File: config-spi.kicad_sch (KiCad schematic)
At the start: 40 parts, among them J1 878321412, Q7 BSS138APW, Q8 BSS138APW, U15 XC7K160T-FFG676, U3 S25FL128SAGNFI000

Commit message: Rebase to Rev. 1.2.2
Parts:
- removed C12: C_47u_0603, data-center-dram-tester-footprints:0603-cap, symbol data-center-dram-tester:C_47u_0603
- removed C13, C37: C_470n_0402, data-center-dram-tester-footprints:0402-cap, symbol data-center-dram-tester:C_470n_0402
- removed C5: C_100n_0402, antmicro-footprints:0402-cap, symbol antmicroCapacitors0402:C_100n_0402
- removed D1, D10: KP-1608CGCK, data-center-dram-tester-footprints:LED_0603, symbol data-center-dram-tester:KP-1608CGCK
- removed D4: TPD6E05U06, data-center-dram-tester-footprints:TPD6E05U06, symbol data-center-dram-tester:TPD6E05U06
- removed EMCCLK1, PUDC_B1: TP_SMD1MM, data-center-dram-tester-footprints:Testpoint_smd_1mm, symbol data-center-dram-tester:TP_SMD1MM
- removed J1: 878321412, antmicro-footprints:PinHeader_2x7_P2mm_SMD_no_locator, symbol antmicroRectangularConnectorsHeadersMalePins:878321412
- removed PROG_B1: B3U-1000P, data-center-dram-tester-footprints:Switch_Tactile_SMD_B3U-1000P, symbol data-center-dram-tester:B3U-1000P
- removed Q7, Q8: BSS138APW, data-center-dram-tester-footprints:SC70-3, symbol data-center-dram-tester:BSS138APW
- removed R10, R33, R34, R36: R_100R_0402, data-center-dram-tester-footprints:0402-res, symbol data-center-dram-tester:R_100R_0402
- removed R11, R12, R13, R23, R24, R26, R27, R58, R59, R60, R9: R_0R_0402, data-center-dram-tester-footprints:0402-res, symbol data-center-dram-tester:R_0R_0402
- removed R14: R_2k2_0402, data-center-dram-tester-footprints:0402-res, symbol data-center-dram-tester:R_2k2_0402
- removed R193: R_10k_0402, antmicro-footprints:0402-res, symbol antmicroResistors0402:R_10k_0402
- removed R21, R22, R28, R32: R_4k7_0402, data-center-dram-tester-footprints:0402-res, symbol data-center-dram-tester:R_4k7_0402
- removed R30, R31, R57: R_330R_0402, data-center-dram-tester-footprints:0402-res, symbol data-center-dram-tester:R_330R_0402
- removed S2: DS04-254-1-01BK-SMT, antmicro-footprints:SW_DS04-254-1-01BK-SMT, symbol antmicroSlideSwitches:DS04-254-1-01BK-SMT
- removed U15: XC7K160T-FFG676, antmicro-footprints:xc7k160tfbg676, symbol data-center-dram-tester:XC7K160T-FFG676
- removed U3: S25FL128SAGNFI000, antmicro-footprints:WSON8x6_WSON6x5_dual, symbol data-center-dram-tester:S25FL128SAGNFI000
- added C12: C_47u_0603, data-center-rdimm-ddr4-tester-footprints:C_0603_1608Metric, symbol data-center-rdimm-ddr4-tester:C_47u_0603
- added C13, C37: C_470n_0402, data-center-rdimm-ddr4-tester-footprints:C_0402_1005Metric, symbol data-center-rdimm-ddr4-tester:C_470n_0402
- added C5: C_100n_0402, data-center-rdimm-ddr4-tester-footprints:C_0402_1005Metric, symbol data-center-rdimm-ddr4-tester:C_100n_0402
- added D1, D10: LED_G_0603_KP-1608CGCK, data-center-rdimm-ddr4-tester-footprints:LED_0603_1608Metric_G, symbol data-center-rdimm-ddr4-tester:LED_G_0603_KP-1608CGCK
- added D4: TPD6E05U06RVZR, data-center-rdimm-ddr4-tester-footprints:USON-14_3.5X1.3X0.5mm_P0.5mm, symbol data-center-rdimm-ddr4-tester:TPD6E05U06RVZR
- added EMCCLK1, PUDC_B1: TP_1mm_SMD, data-center-rdimm-ddr4-tester-footprints:Testpoint_smd_1mm, symbol data-center-rdimm-ddr4-tester:TP_1mm_SMD
- added J1: PinHeader_2x7_P2mm_SMD_Shrouded_no-locator, data-center-rdimm-ddr4-tester-footprints:PinHeader_2x7_P2mm_SMD_Shrouded_no-locator, symbol data-center-rdimm-ddr4-tester:PinHeader_2x7_P2mm_SMD_Shrouded_no-locator
- added PROG_B1: SW_B3U-1000P, data-center-rdimm-ddr4-tester-footprints:SW_B3U-3000P, symbol data-center-rdimm-ddr4-tester:SW_B3U-1000P
- added Q7, Q8: BSS138PW, data-center-rdimm-ddr4-tester-footprints:SC70-3, symbol data-center-rdimm-ddr4-tester:BSS138PW
- added R10, R33, R34, R36: R_100R_0402, data-center-rdimm-ddr4-tester-footprints:R_0402_1005Metric, symbol data-center-rdimm-ddr4-tester:R_100R_0402
- added R11, R12, R13, R23, R24, R26, R27, R58, R59, R60, R9: R_0R_0402, data-center-rdimm-ddr4-tester-footprints:R_0402_1005Metric, symbol data-center-rdimm-ddr4-tester:R_0R_0402
- added R14: R_2k2_0402, data-center-rdimm-ddr4-tester-footprints:R_0402_1005Metric, symbol data-center-rdimm-ddr4-tester:R_2k2_0402
- added R193: R_10k_0402, data-center-rdimm-ddr4-tester-footprints:R_0402_1005Metric, symbol data-center-rdimm-ddr4-tester:R_10k_0402
- added R21, R22, R28, R32: R_4k7_0402, data-center-rdimm-ddr4-tester-footprints:R_0402_1005Metric, symbol data-center-rdimm-ddr4-tester:R_4k7_0402
- added R30, R31, R57: R_330R_0402, data-center-rdimm-ddr4-tester-footprints:R_0402_1005Metric, symbol data-center-rdimm-ddr4-tester:R_330R_0402
- added S2: SW_DS04-254-1-01BK-SMT, data-center-rdimm-ddr4-tester-footprints:SW_DS04-254-1-01BK-SMT, symbol data-center-rdimm-ddr4-tester:SW_DS04-254-1-01BK-SMT
- added U15: XC7K160T-FFG676, data-center-rdimm-ddr4-tester-footprints:BGA-676_27x27mm_Layout26x26_P1X1mm, symbol data-center-rdimm-ddr4-tester:XC7K160T-FFG676
- added U3: S25FL128SAGNFI000, data-center-rdimm-ddr4-tester-footprints:WSON-8_6x8x0.5mm_P1.27mm, symbol data-center-rdimm-ddr4-tester:S25FL128SAGNFI000
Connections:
- net 3V3_SYS: now also C12.1, C13.1, C37.1, C5.1, D1.1, D10.1, J1.2, R10.1, R12.2, R14.1, R193.2, R21.1, R22.1, R28.1, R32.1, R33.1, R57.1, R58.1, R9.2, U15.L7 (VCCO_0), U15.T6 (VCCO_0), U3.8 (V_{CC})
- net CCLK: now also R24.2, R33.2, R34.1, U15.C8 (CCLK_0)
- net CFGBVS: now also R58.2, U15.P7 (CFGBVS_0)
- net DONE: now also Q7.1 (G), R57.2, U15.J7 (DONE_0)
- net EMCCLK: now also EMCCLK1.1
- net FCS_B: now also R14.2, R23.2
- net GND: now also C12.2, C13.2, C37.2, C5.2, D4.10 (GND), D4.5 (GND), J1.1, J1.11, J1.13, J1.3, J1.5, J1.7, J1.9, PROG_B1.2, Q7.2 (S), Q8.2 (S), R11.2, R13.2, R34.2, R36.2, S2.2, U15.N11 (VREFN_0), U15.N12 (VP_0), U15.P11 (VN_0), U15.P12 (VREFP_0), U15.R11 (DXN_0), U15.R12 (DXP_0), U3.4 (V_{SS})
- net INIT_B: now also Q8.1 (G), R28.2, U15.G7 (INIT_B_0)
- net MODE0: now also R11.1, R9.1, U15.T5 (M0_0)
- net MODE1: now also R12.1, R13.1, U15.T2 (M1_0)
- net MODE2: now also R193.1, S2.1, U15.P5 (M2_0)
- net PROGRAM_B: now also PROG_B1.1, R32.2, U15.P6 (PROGRAM_B_0)
- net PUDC_B: now also PUDC_B1.1, R10.2, R36.1
- net QSPI_DQ0: now also R59.2
- net QSPI_DQ1: now also R60.2
- net QSPI_DQ2: now also R22.2, R27.2
- net QSPI_DQ3: now also R21.2, R26.2
- net TCK_JTAG: now also D4.13 (D1-), D4.2 (D1-), J1.6, U15.L8 (TCK_0)
- net TDI_JTAG: now also D4.7 (D3-), D4.8 (D3-), J1.10, U15.R6 (TDI_0)
- net TDO_JTAG: now also D4.6 (D3+), D4.9 (D3+), J1.8, U15.R7 (TDO_0)
- net TMS_JTAG: now also D4.1 (D1+), D4.14 (D1+), J1.4, U15.N8 (TMS_0)
- new net: D4.11 (D2-), D4.4 (D2-)
- new net: D4.12 (D2+), D4.3 (D2+)
- new net: R23.1, U3.1 (~{CS})
- new net: R60.1, U3.2 (SO/IO1)
- new net: R27.1, U3.3 (~{WP}/IO2)
- new net: R59.1, U3.5 (SI/IO0)
- new net: R24.1, U3.6 (SCK)
- new net: R26.1, U3.7 (~{HOLD}/IO3)
- new net: D1.2, R30.1
- new net: Q7.3 (D), R30.2
- new net: D10.2, R31.1
- new net: Q8.3 (D), R31.2
- no-connect marks 2 -> 4
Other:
- note added: "000 001 010 100 101 110 111"
- note added: "Config. mode"
- note added: "MODE[2:0]"
- note added: "Master Serial Master SPI Master BPI Master SelectMAP JTAG Slave SelectMAP Slave Serial"
- note removed: "Config. mode Master Serial Master SPI Master BPI Master SelectMAP JTAG Slave SelectMAP Slave Serial"
- note removed: "MODE[2:0] 000 001 010 100 101 110 111"

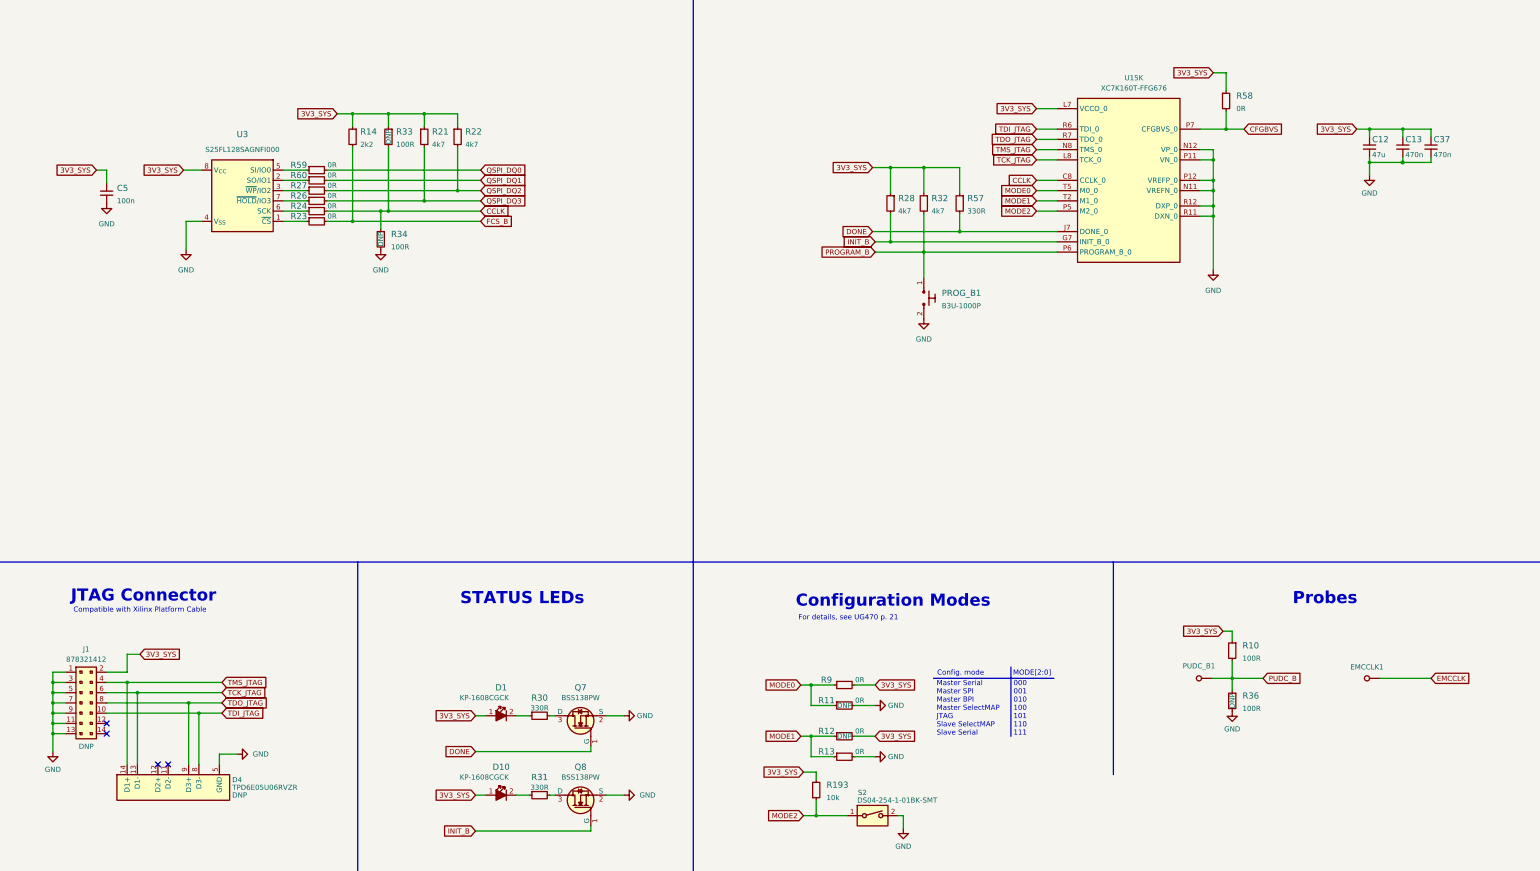
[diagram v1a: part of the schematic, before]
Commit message: Update designators and sync schematic with PCB
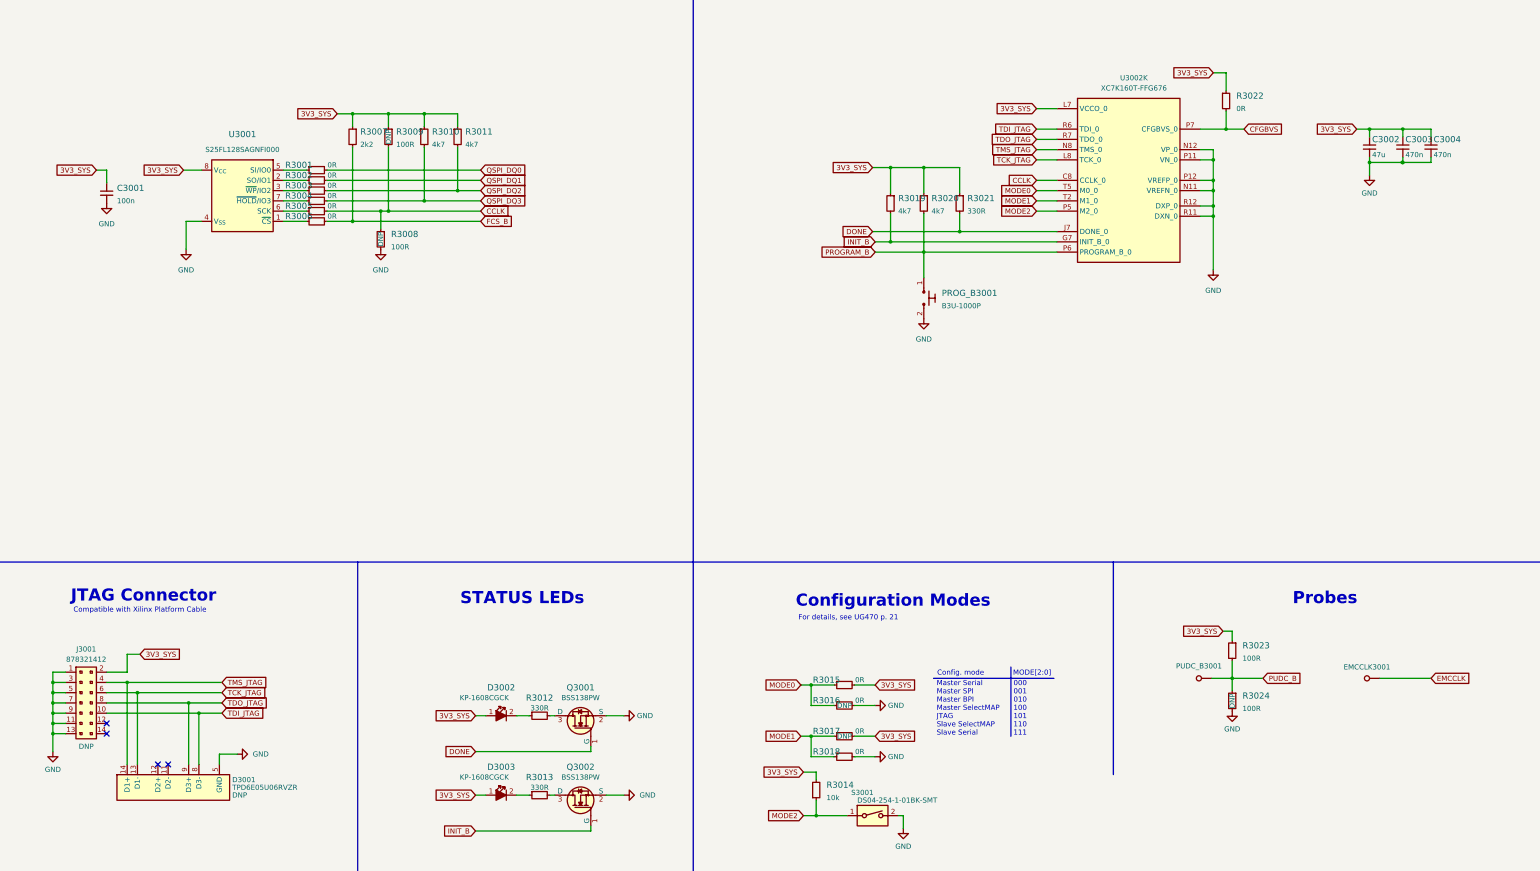
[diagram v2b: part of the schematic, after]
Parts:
- renumbered C5 to C3001, C12 to C3002, C13 to C3003, C37 to C3004, D4 to D3001, D1 to D3002, D10 to D3003, EMCCLK1 to EMCCLK3001, J1 to J3001, PROG_B1 to PROG_B3001, PUDC_B1 to PUDC_B3001, Q7 to Q3001, Q8 to Q3002, R59 to R3001, R60 to R3002, R27 to R3003, R26 to R3004, R24 to R3005, R23 to R3006, R14 to R3007, R34 to R3008, R33 to R3009, R21 to R3010, R22 to R3011, R30 to R3012, R31 to R3013, R193 to R3014, R9 to R3015, R11 to R3016, R12 to R3017, R13 to R3018, R28 to R3019, R32 to R3020, R57 to R3021, R58 to R3022, R10 to R3023, R36 to R3024, S2 to S3001, U3 to U3001, U15 to U3002

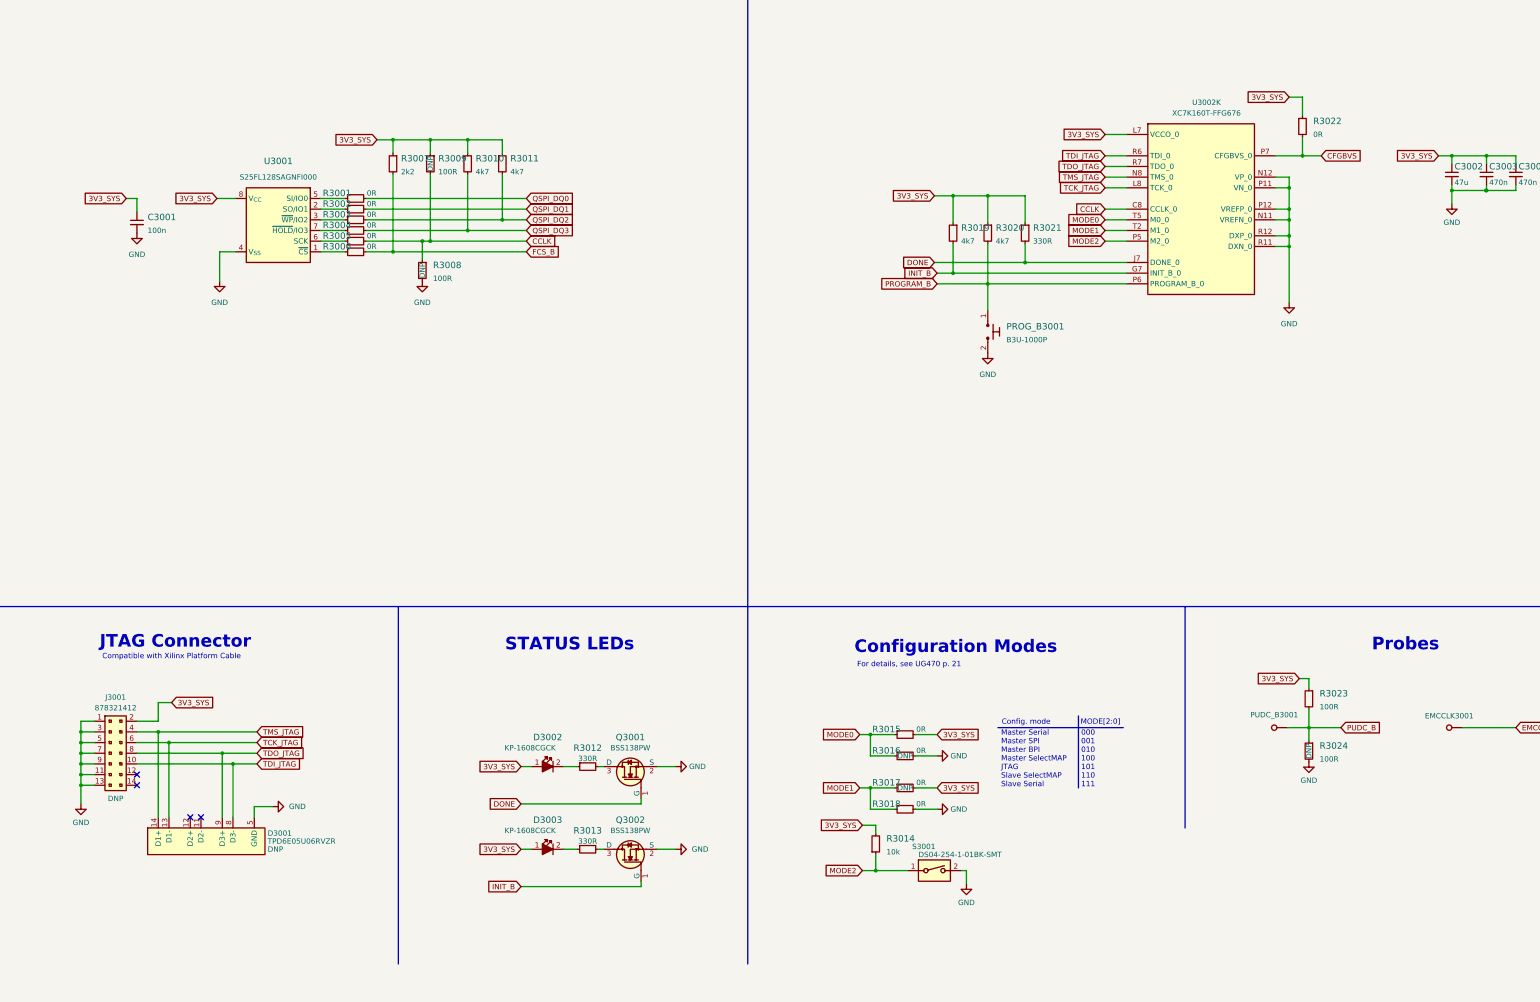
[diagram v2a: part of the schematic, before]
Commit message: Replace supply labels with proper symbols
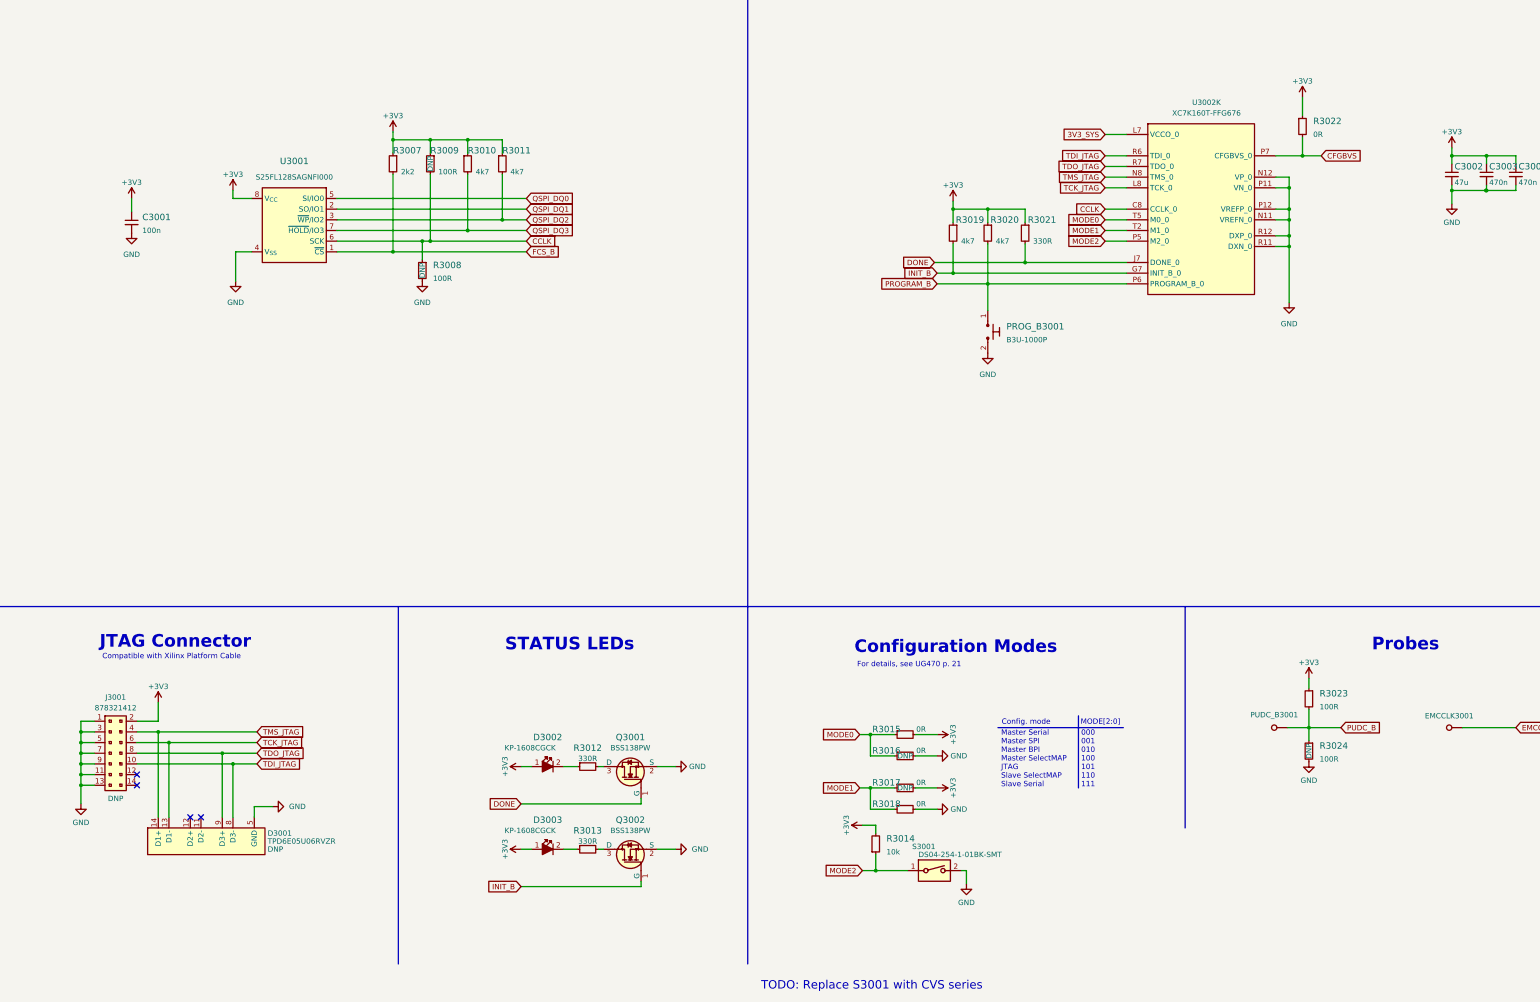
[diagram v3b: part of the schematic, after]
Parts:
- removed R3001, R3002, R3003, R3004, R3005, R3006: R_0R_0402, data-center-rdimm-ddr4-tester-footprints:R_0402_1005Metric, symbol data-center-rdimm-ddr4-tester:R_0R_0402
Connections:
- net 3V3_SYS: no longer C3001.1, C3002.1, C3003.1, C3004.1, D3002.1, D3003.1, J3001.2, R3007.1, R3009.1, R3010.1, R3011.1, R3014.2, R3015.2, R3017.2, R3019.1, R3020.1, R3021.1, R3022.1, R3023.1, U3001.8 (V_{CC})
- net CCLK: now also U3001.6 (SCK)
- net FCS_B: now also U3001.1 (~{CS})
- net QSPI_DQ0: now also U3001.5 (SI/IO0)
- net QSPI_DQ1: now also U3001.2 (SO/IO1)
- net QSPI_DQ2: now also U3001.3 (~{WP}/IO2)
- net QSPI_DQ3: now also U3001.7 (~{HOLD}/IO3)
- new net +3V3: C3001.1, C3002.1, C3003.1, C3004.1, D3002.1, D3003.1, J3001.2, R3007.1, R3009.1, R3010.1, R3011.1, R3014.2, R3015.2, R3017.2, R3019.1, R3020.1, R3021.1, R3022.1, R3023.1, U3001.8 (V_{CC})
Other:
- note added: "TODO: Replace S3001 with CVS series"
- moved on the sheet: C3001, U3001
